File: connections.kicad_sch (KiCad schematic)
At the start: 31 parts

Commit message: Finished circuit
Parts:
- removed Conn?: FlipButton, symbol Scout_library:B2B_VERT_1.5MM
- removed Conn?: Button3, symbol Scout_library:B2B_VERT_1.5MM
- removed Conn?: Button4, symbol Scout_library:B2B_VERT_1.5MM
- removed Conn?: Button6, symbol Scout_library:B2B_VERT_1.5MM
- removed Conn?: Button5, symbol Scout_library:B2B_VERT_1.5MM
- removed Conn?: CaptureButton, symbol Scout_library:B2B_VERT_1.5MM
- added Conn10, Conn11, Conn5, Conn7, Conn8, Conn9: FlipButton, symbol Scout_library:B2B_VERT_1.5MM
- added S1, S2, S3, S4, S5, S6: TL3315NF160Q, digikey-footprints:Switch_Tactile_SMD_4.5x4.5mm_TL3315NF160Q, symbol dk_Tactile-Switches:TL3315NF160Q
- gave numbers to parts that had none: 25
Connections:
- net +3.3V: now also Q1.1, Q2.1, Conn10.1 (Pin_1), Conn11.1 (Pin_1), Conn5.1 (Pin_1), Conn7.1 (Pin_1), Conn8.1 (Pin_1), Conn9.1 (Pin_1), S1.1, S2.1, S3.1, S4.1, S5.1, S6.1
- net Button3: now also Conn8.2 (Pin_2), S3.4
- net Button4: now also Conn9.2 (Pin_2), S4.4
- net Button5: now also Conn10.2 (Pin_2), S5.4
- net Button6: now also Conn11.2 (Pin_2), S6.4
- net CaptureButton: now also Conn7.2 (Pin_2), S2.4
- net FlipButton: now also Conn5.2 (Pin_2), S1.4
- no-connect marks 0 -> 12
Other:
- moved on the sheet: Conn3, Conn4, Conn6, J1, J2, MOSFET1, MOSFET2, Q1, Q2, R10, R11, R5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

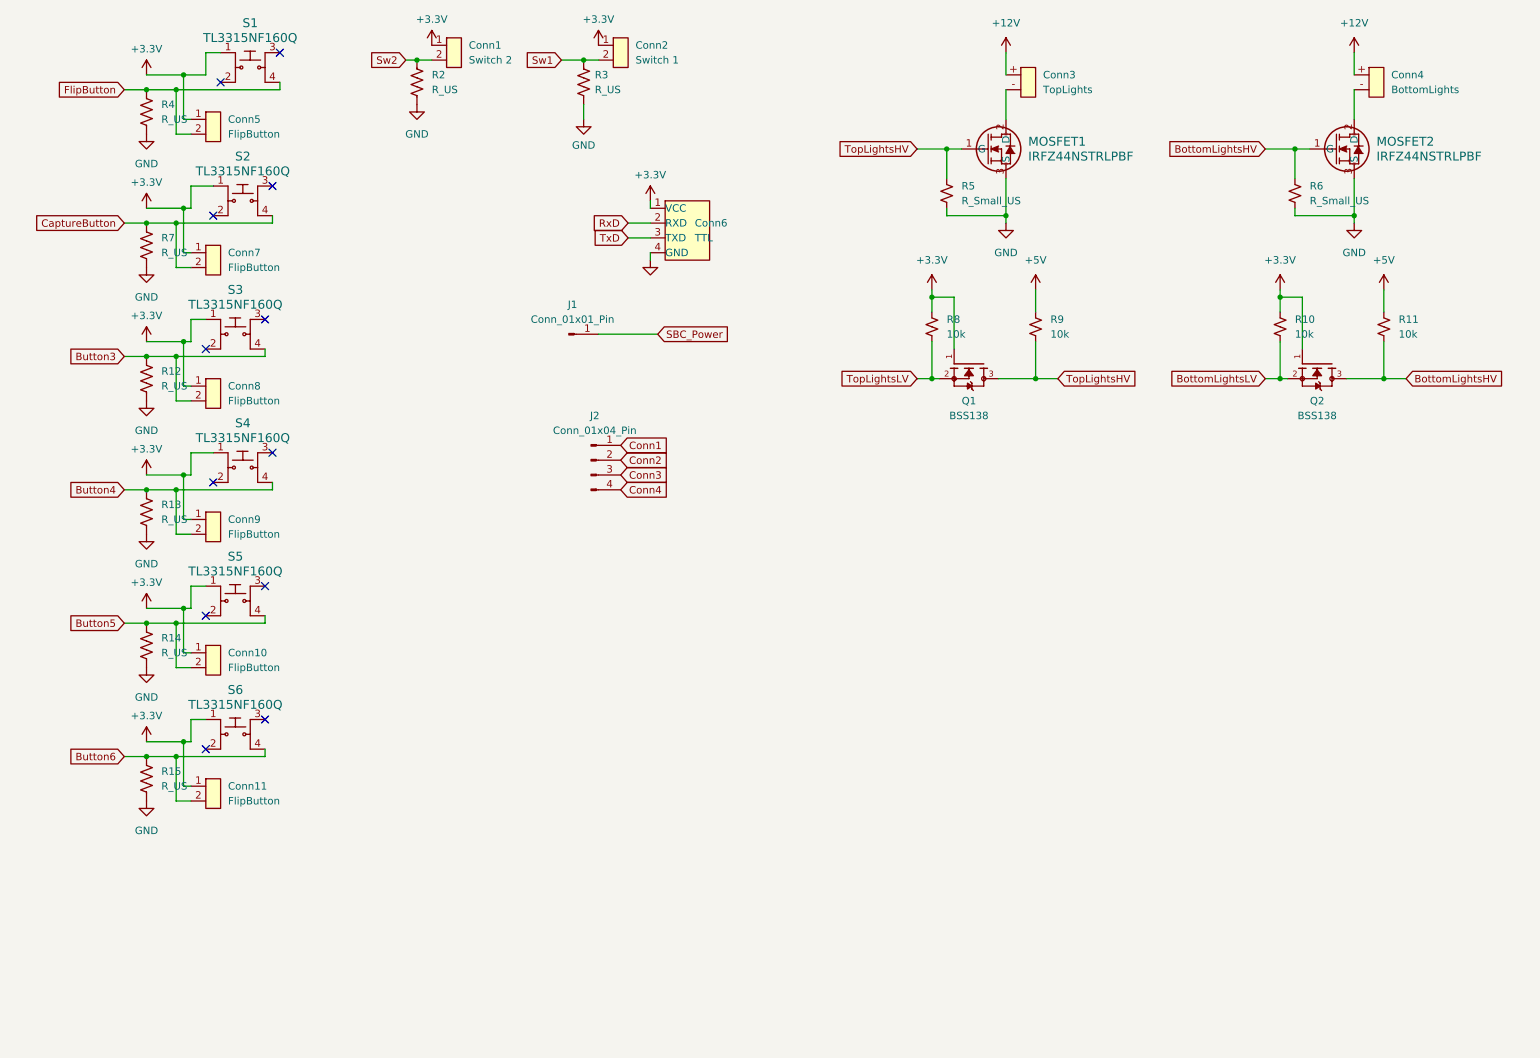
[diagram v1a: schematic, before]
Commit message: Updated the footprints for all the components.
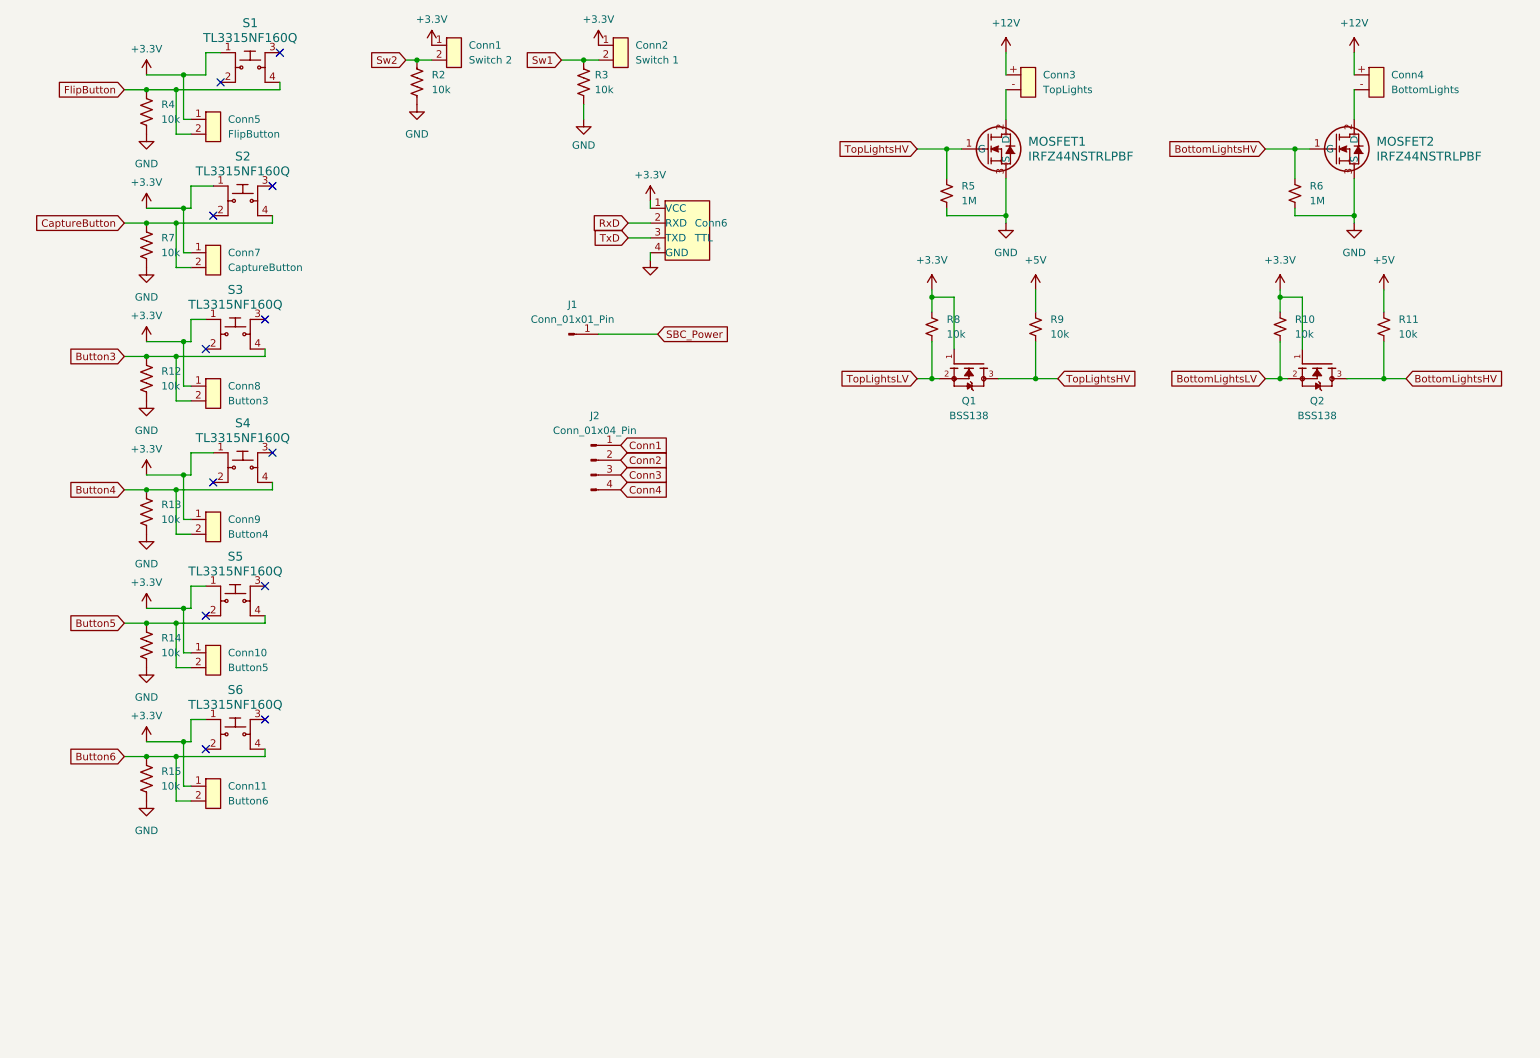
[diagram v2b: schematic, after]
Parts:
- Conn1, Conn2, Conn3, Conn4, Conn5: footprint (none) -> Downloaded_footprints:CONN_B2B-ZRLFSN_JST
- Conn10: value FlipButton -> Button5; footprint (none) -> Downloaded_footprints:CONN_B2B-ZRLFSN_JST
- Conn11: value FlipButton -> Button6; footprint (none) -> Downloaded_footprints:CONN_B2B-ZRLFSN_JST
- Conn6: footprint (none) -> Downloaded_footprints:CONN_B4B-ZRLFSN_JST
- Conn7: value FlipButton -> CaptureButton; footprint (none) -> Downloaded_footprints:CONN_B2B-ZRLFSN_JST
- Conn8: value FlipButton -> Button3; footprint (none) -> Downloaded_footprints:CONN_B2B-ZRLFSN_JST
- Conn9: value FlipButton -> Button4; footprint (none) -> Downloaded_footprints:CONN_B2B-ZRLFSN_JST
- R10, R11, R8, R9: footprint (none) -> Resistor_SMD:R_0603_1608Metric_Pad0.98x0.95mm_HandSolder
- R12, R13, R14, R15, R2, R3, R4, R7: value R_US -> 10k; footprint (none) -> Resistor_SMD:R_0603_1608Metric_Pad0.98x0.95mm_HandSolder
- R5, R6: value R_Small_US -> 1M; footprint (none) -> Resistor_SMD:R_0603_1608Metric_Pad0.98x0.95mm_HandSolder

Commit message: PCB Layout done
Routing yet to do.
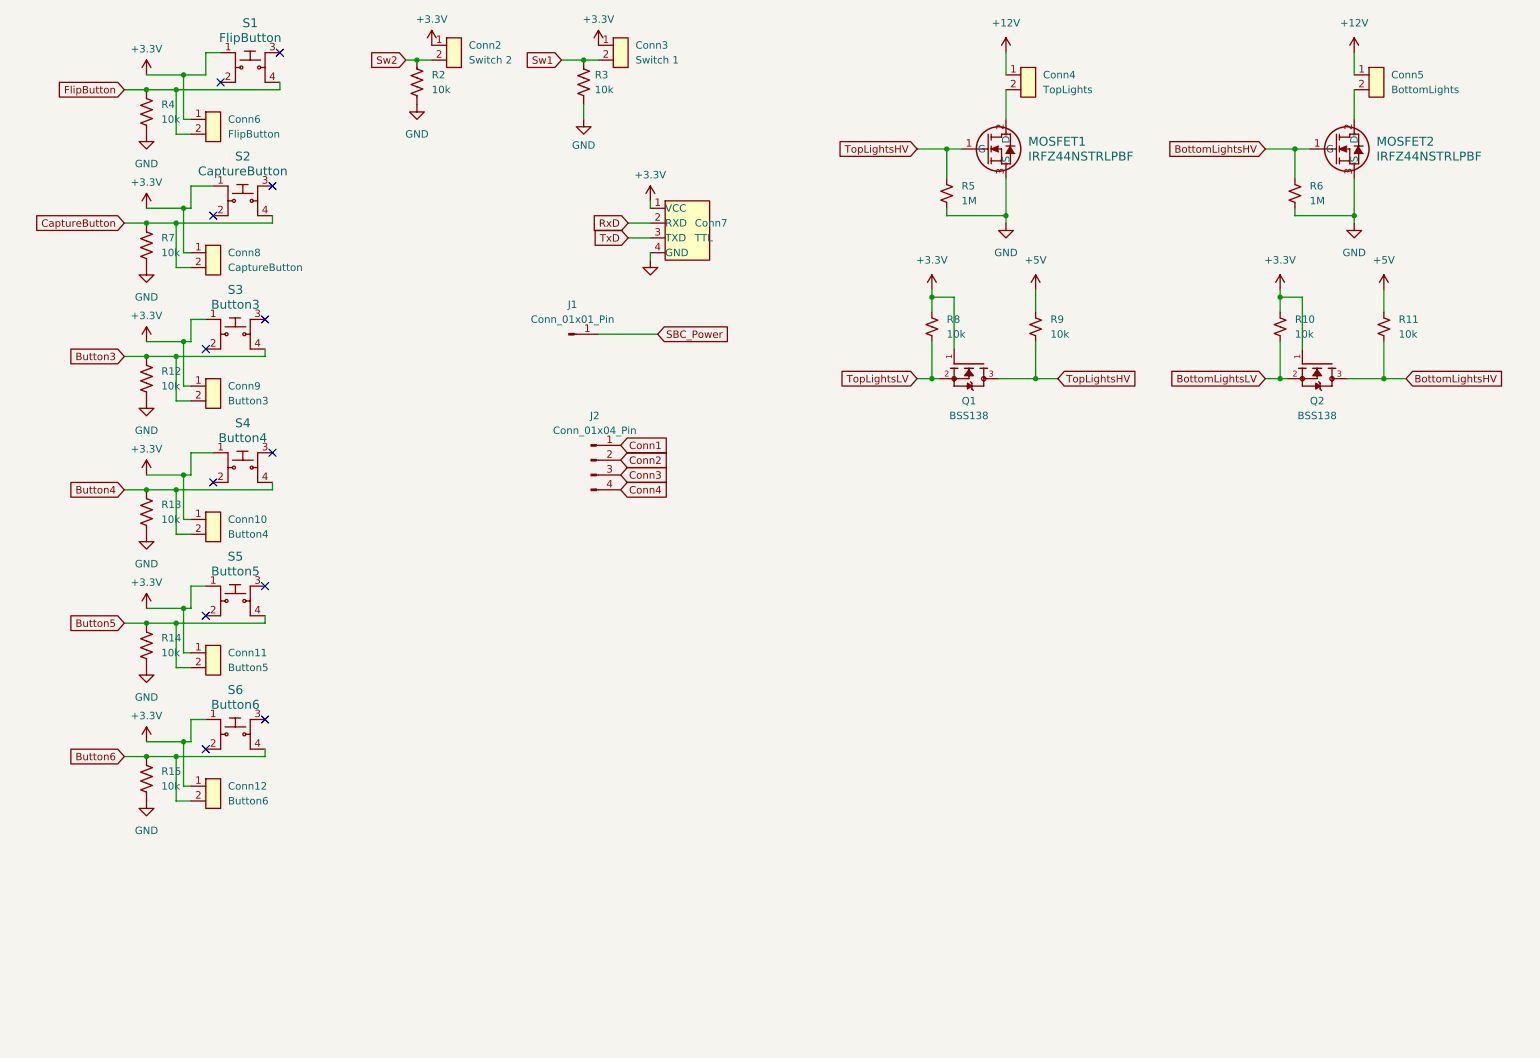
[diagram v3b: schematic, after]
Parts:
- Q1, Q2: footprint BSS138:SOT95P240X111-3N -> Downloaded_footprints:SOT95P240X111-3N
- S1: value TL3315NF160Q -> FlipButton
- S2: value TL3315NF160Q -> CaptureButton
- S3: value TL3315NF160Q -> Button3
- S4: value TL3315NF160Q -> Button4
- S5: value TL3315NF160Q -> Button5
- S6: value TL3315NF160Q -> Button6
- renumbered Conn9 to Conn10, Conn10 to Conn11, Conn11 to Conn12, Conn1 to Conn2, Conn2 to Conn3, Conn3 to Conn4, Conn4 to Conn5, Conn5 to Conn6, Conn6 to Conn7, Conn7 to Conn8, Conn8 to Conn9
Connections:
- net +12V: now also Conn4.1 (Pin_1), Conn5.1 (Pin_1); no longer Conn4.+ (Pin_1), Conn5.+ (Pin_1)
- net at MOSFET2.2 (D): now also Conn5.2 (Pin_2); no longer Conn5.- (Pin_2)
- net at MOSFET1.2 (D): now also Conn4.2 (Pin_2); no longer Conn4.- (Pin_2)
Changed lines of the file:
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@@
   (symbol (lib_name "B4B_VERT_1.5MM_1") (lib_id "Scout_library:B4B_VERT_1.5MM") (at 128.27 52.07 0) (unit 1)
     (in_bom yes) (on_board yes) (dnp no) (fields_autoplaced)
-    (property "Reference" "Conn6" (at 132.08 57.15 0)
+    (property "Reference" "Conn7" (at 132.08 57.15 0)
       (effects (font (size 1.27 1.27)) (justify left))
     )
@@
       (project "Scout_Board"
         (path "/e58a9779-147f-4c0c-a745-6e9bc8ec0357/1c50300d-eb18-4ae0-a965-4e91fdf6ec14"
-          (reference "Conn6") (unit 1)
+          (reference "Conn7") (unit 1)
         )
       )
@@
       (effects (font (size 1.524 1.524)))
     )
-    (property "Value" "TL3315NF160Q" (at 53.34 139.7 0)
+    (property "Value" "Button6" (at 53.34 139.7 0)
       (effects (font (size 1.524 1.524)))
     )
@@
   (symbol (lib_id "Scout_library:B2B_VERT_1.5MM") (at 49.53 59.69 0) (unit 1)
     (in_bom yes) (on_board yes) (dnp no) (fields_autoplaced)
-    (property "Reference" "Conn7" (at 52.07 62.23 0)
+    (property "Reference" "Conn8" (at 52.07 62.23 0)
       (effects (font (size 1.27 1.27)) (justify left))
     )
@@
       (project "Scout_Board"
         (path "/e58a9779-147f-4c0c-a745-6e9bc8ec0357/1c50300d-eb18-4ae0-a965-4e91fdf6ec14"
-          (reference "Conn7") (unit 1)
+          (reference "Conn8") (unit 1)
         )
       )
@@
       (effects (font (size 1.524 1.524)))
     )
-    (property "Value" "TL3315NF160Q" (at 53.34 116.84 0)
+    (property "Value" "Button5" (at 53.34 116.84 0)
       (effects (font (size 1.524 1.524)))
     )
@@
   (symbol (lib_id "Scout_library:B2B_VERT_1.5MM") (at 49.53 151.13 0) (unit 1)
     (in_bom yes) (on_board yes) (dnp no) (fields_autoplaced)
-    (property "Reference" "Conn11" (at 52.07 153.67 0)
+    (property "Reference" "Conn12" (at 52.07 153.67 0)
       (effects (font (size 1.27 1.27)) (justify left))
     )
@@
       (project "Scout_Board"
         (path "/e58a9779-147f-4c0c-a745-6e9bc8ec0357/1c50300d-eb18-4ae0-a965-4e91fdf6ec14"
-          (reference "Conn11") (unit 1)
+          (reference "Conn12") (unit 1)
         )
       )
@@
       (effects (font (size 1.27 1.27)))
     )
-    (property "Footprint" "BSS138:SOT95P240X111-3N" (at 238.76 81.28 0)
+    (property "Footprint" "Downloaded_footprints:SOT95P240X111-3N" (at 238.76 81.28 0)
       (effects (font (size 1.27 1.27)) (justify bottom) hide)
     )
@@
   (symbol (lib_id "Scout_library:B2B_VERT_1.5MM") (at 90.805 24.13 0) (unit 1)
     (in_bom yes) (on_board yes) (dnp no) (fields_autoplaced)
-    (property "Reference" "Conn1" (at 93.345 26.67 0)
+    (property "Reference" "Conn2" (at 93.345 26.67 0)
       (effects (font (size 1.27 1.27)) (justify left))
     )
@@
       (project "Scout_Board"
         (path "/e58a9779-147f-4c0c-a745-6e9bc8ec0357/1c50300d-eb18-4ae0-a965-4e91fdf6ec14"
-          (reference "Conn1") (unit 1)
+          (reference "Conn2") (unit 1)
         )
       )
@@
   (symbol (lib_id "Scout_library:B2B_VERT_1.5MM") (at 119.38 24.13 0) (unit 1)
     (in_bom yes) (on_board yes) (dnp no) (fields_autoplaced)
-    (property "Reference" "Conn2" (at 121.92 26.67 0)
+    (property "Reference" "Conn3" (at 121.92 26.67 0)
       (effects (font (size 1.27 1.27)) (justify left))
     )
@@
       (project "Scout_Board"
         (path "/e58a9779-147f-4c0c-a745-6e9bc8ec0357/1c50300d-eb18-4ae0-a965-4e91fdf6ec14"
-          (reference "Conn2") (unit 1)
+          (reference "Conn3") (unit 1)
         )
       )
@@
   (symbol (lib_id "Scout_library:B2B_VERT_1.5MM") (at 49.53 36.83 0) (unit 1)
     (in_bom yes) (on_board yes) (dnp no) (fields_autoplaced)
-    (property "Reference" "Conn5" (at 52.07 39.37 0)
+    (property "Reference" "Conn6" (at 52.07 39.37 0)
       (effects (font (size 1.27 1.27)) (justify left))
     )
@@
       (project "Scout_Board"
         (path "/e58a9779-147f-4c0c-a745-6e9bc8ec0357/1c50300d-eb18-4ae0-a965-4e91fdf6ec14"
-          (reference "Conn5") (unit 1)
+          (reference "Conn6") (unit 1)
         )
       )
@@
     )
   )
-  (symbol (lib_name "B2B_VERT_1.5MM_1") (lib_id "Scout_library:B2B_VERT_1.5MM") (at 189.23 29.21 0) (unit 1)
-    (in_bom yes) (on_board yes) (dnp no) (fields_autoplaced)
-    (property "Reference" "Conn3" (at 191.77 31.75 0)
+  (symbol (lib_name "B2B_VERT_1.5MM_2") (lib_id "Scout_library:B2B_VERT_1.5MM") (at 189.23 29.21 0) (unit 1)
+    (in_bom yes) (on_board yes) (dnp no) (fields_autoplaced)
+    (property "Reference" "Conn4" (at 191.77 31.75 0)
       (effects (font (size 1.27 1.27)) (justify left))
     )
@@
       (effects (font (size 1.27 1.27)) hide)
     )
-    (pin "+")
-    (pin "-")
-    (instances
-      (project "Scout_Board"
-        (path "/e58a9779-147f-4c0c-a745-6e9bc8ec0357/1c50300d-eb18-4ae0-a965-4e91fdf6ec14"
-          (reference "Conn3") (unit 1)
+    (pin "1")
+    (pin "2")
+    (instances
+      (project "Scout_Board"
+        (path "/e58a9779-147f-4c0c-a745-6e9bc8ec0357/1c50300d-eb18-4ae0-a965-4e91fdf6ec14"
+          (reference "Conn4") (unit 1)
         )
       )
@@
   (symbol (lib_id "Scout_library:B2B_VERT_1.5MM") (at 49.53 105.41 0) (unit 1)
     (in_bom yes) (on_board yes) (dnp no) (fields_autoplaced)
-    (property "Reference" "Conn9" (at 52.07 107.95 0)
+    (property "Reference" "Conn10" (at 52.07 107.95 0)
       (effects (font (size 1.27 1.27)) (justify left))
     )
@@
       (project "Scout_Board"
         (path "/e58a9779-147f-4c0c-a745-6e9bc8ec0357/1c50300d-eb18-4ae0-a965-4e91fdf6ec14"
-          (reference "Conn9") (unit 1)
+          (reference "Conn10") (unit 1)
         )
       )
@@
       (effects (font (size 1.524 1.524)))
     )
-    (property "Value" "TL3315NF160Q" (at 53.34 71.12 0)
+    (property "Value" "Button3" (at 53.34 71.12 0)
       (effects (font (size 1.524 1.524)))
     )
@@
   (symbol (lib_id "Scout_library:B2B_VERT_1.5MM") (at 49.53 128.27 0) (unit 1)
     (in_bom yes) (on_board yes) (dnp no) (fields_autoplaced)
-    (property "Reference" "Conn10" (at 52.07 130.81 0)
+    (property "Reference" "Conn11" (at 52.07 130.81 0)
       (effects (font (size 1.27 1.27)) (justify left))
     )
@@
       (project "Scout_Board"
         (path "/e58a9779-147f-4c0c-a745-6e9bc8ec0357/1c50300d-eb18-4ae0-a965-4e91fdf6ec14"
-          (reference "Conn10") (unit 1)
+          (reference "Conn11") (unit 1)
         )
       )
@@
       (effects (font (size 1.524 1.524)))
     )
-    (property "Value" "TL3315NF160Q" (at 54.61 48.26 0)
+    (property "Value" "CaptureButton" (at 54.61 48.26 0)
       (effects (font (size 1.524 1.524)))
     )
@@
   (symbol (lib_name "B2B_VERT_1.5MM_1") (lib_id "Scout_library:B2B_VERT_1.5MM") (at 248.92 29.21 0) (unit 1)
     (in_bom yes) (on_board yes) (dnp no) (fields_autoplaced)
-    (property "Reference" "Conn4" (at 251.46 31.75 0)
+    (property "Reference" "Conn5" (at 251.46 31.75 0)
       (effects (font (size 1.27 1.27)) (justify left))
     )
@@
       (effects (font (size 1.27 1.27)) hide)
     )
-    (pin "+")
-    (pin "-")
-    (instances
-      (project "Scout_Board"
-        (path "/e58a9779-147f-4c0c-a745-6e9bc8ec0357/1c50300d-eb18-4ae0-a965-4e91fdf6ec14"
-          (reference "Conn4") (unit 1)
+    (pin "1")
+    (pin "2")
+    (instances
+      (project "Scout_Board"
+        (path "/e58a9779-147f-4c0c-a745-6e9bc8ec0357/1c50300d-eb18-4ae0-a965-4e91fdf6ec14"
+          (reference "Conn5") (unit 1)
         )
       )
@@
       (effects (font (size 1.524 1.524)))
     )
-    (property "Value" "TL3315NF160Q" (at 55.88 25.4 0)
+    (property "Value" "FlipButton" (at 55.88 25.4 0)
       (effects (font (size 1.524 1.524)))
     )
@@
       (effects (font (size 1.524 1.524)))
     )
-    (property "Value" "TL3315NF160Q" (at 54.61 93.98 0)
+    (property "Value" "Button4" (at 54.61 93.98 0)
       (effects (font (size 1.524 1.524)))
     )
@@
       (effects (font (size 1.27 1.27)))
     )
-    (property "Footprint" "BSS138:SOT95P240X111-3N" (at 179.07 81.28 0)
+    (property "Footprint" "Downloaded_footprints:SOT95P240X111-3N" (at 179.07 81.28 0)
       (effects (font (size 1.27 1.27)) (justify bottom) hide)
     )
@@
   (symbol (lib_id "Scout_library:B2B_VERT_1.5MM") (at 49.53 82.55 0) (unit 1)
     (in_bom yes) (on_board yes) (dnp no) (fields_autoplaced)
-    (property "Reference" "Conn8" (at 52.07 85.09 0)
+    (property "Reference" "Conn9" (at 52.07 85.09 0)
       (effects (font (size 1.27 1.27)) (justify left))
     )
@@
       (project "Scout_Board"
         (path "/e58a9779-147f-4c0c-a745-6e9bc8ec0357/1c50300d-eb18-4ae0-a965-4e91fdf6ec14"
-          (reference "Conn8") (unit 1)
-        )
-      )
+          (reference "Conn9") (unit 1)
+        )
+      )
